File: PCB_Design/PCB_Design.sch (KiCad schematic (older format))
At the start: 10 parts, among them J1 TP4056

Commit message: Hojas en el esquemático
Se añadió como hoja independiente el cargador de la batería al esquemático.
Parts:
- removed BT: Battery_Cell, symbol Device:Battery_Cell
- removed C1, C2: 10u, symbol Device:C
- removed J1: TP4056, SOIC127P600X175-9N, symbol TP4056:TP4056
- removed R_5v: 0.4, symbol Device:R
- removed R_PROG: R, symbol Device:R
- removed R_gLED, R_rLED: 1k, symbol Device:R
- removed gLED, rLED: LED, symbol Device:LED
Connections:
- net labels removed: +5V, GND
- wire segments 25 -> 0
- no-connect marks 2 -> 0

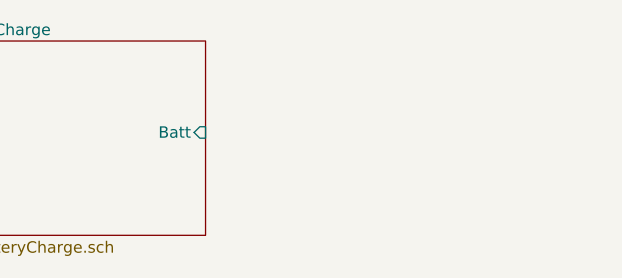
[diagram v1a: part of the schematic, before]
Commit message: Creación de la hoja de regulación de tensión
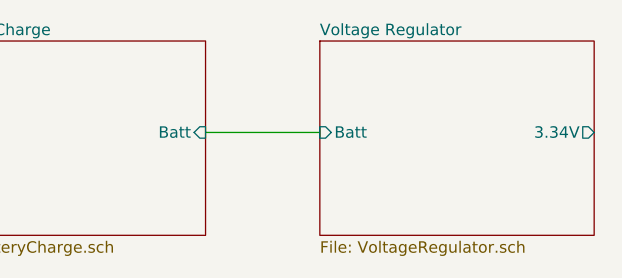
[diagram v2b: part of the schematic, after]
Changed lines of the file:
@@
 $Descr A4 11693 8268
 encoding utf-8
-Sheet 1 2
+Sheet 1 3
 Title ""
 Date ""
@@
 F2 "Batt" I R 3550 2100 50
 $EndSheet
+$Sheet
+S 4050 1700 1200 850
+U 619FB45F
+F0 "Voltage Regulator" 50
+F1 "VoltageRegulator.sch" 50
+F2 "Batt" I L 4050 2100 50
+F3 "3.34V" O R 5250 2100 50
+$EndSheet
+Wire Wire Line
+	3550 2100 4050 2100
 $EndSCHEMATC

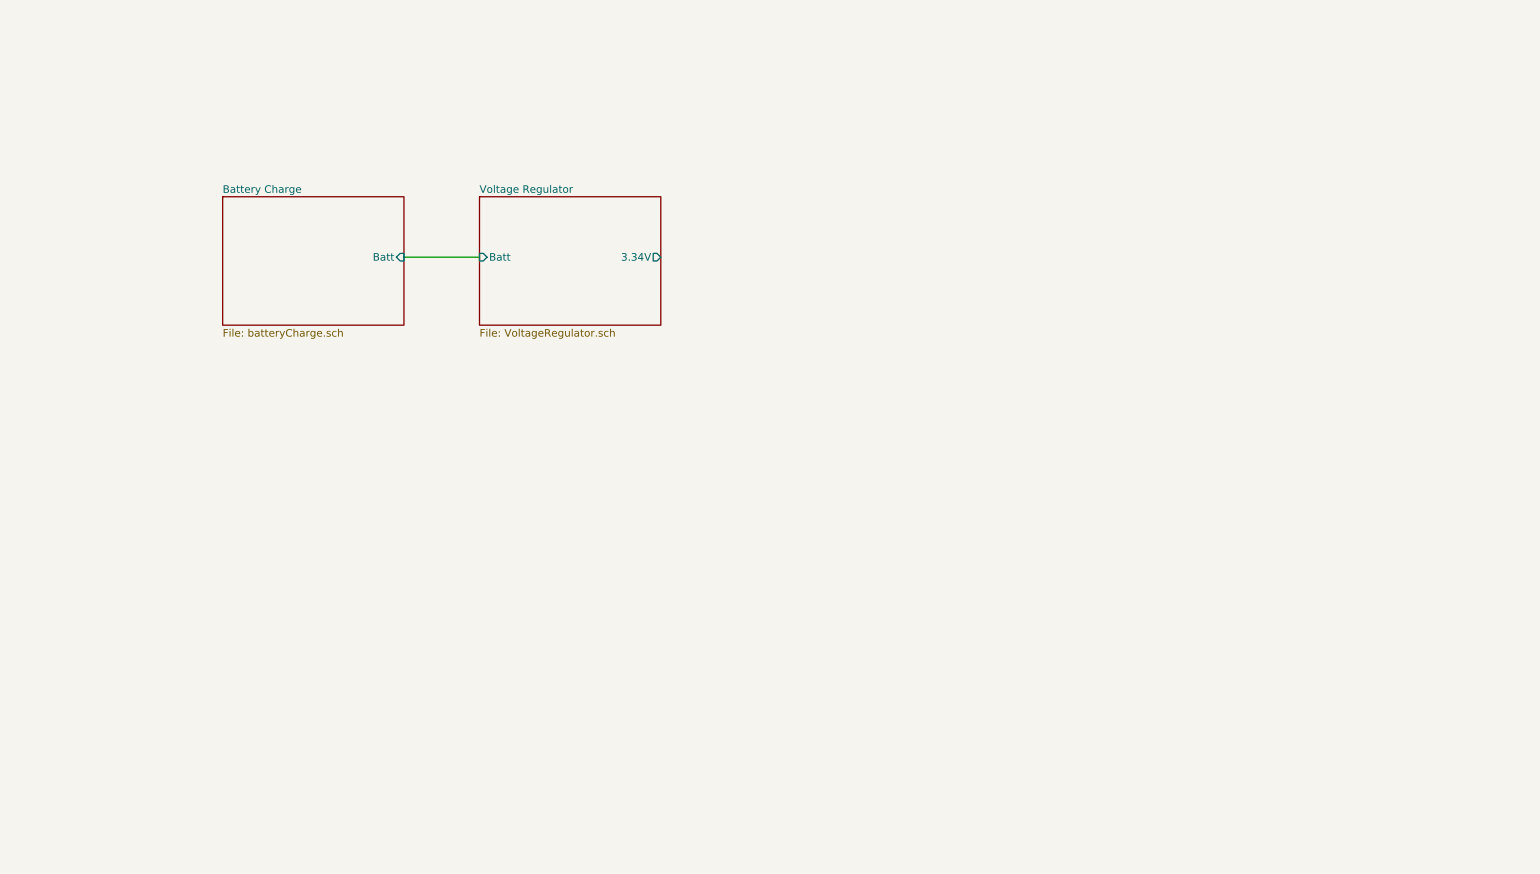
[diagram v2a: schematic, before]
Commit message: Programación por UART-Botones
Se añadieron los botones con el circuito de debouncing, un botón de enable para la esp32 y los pines para la programacion.
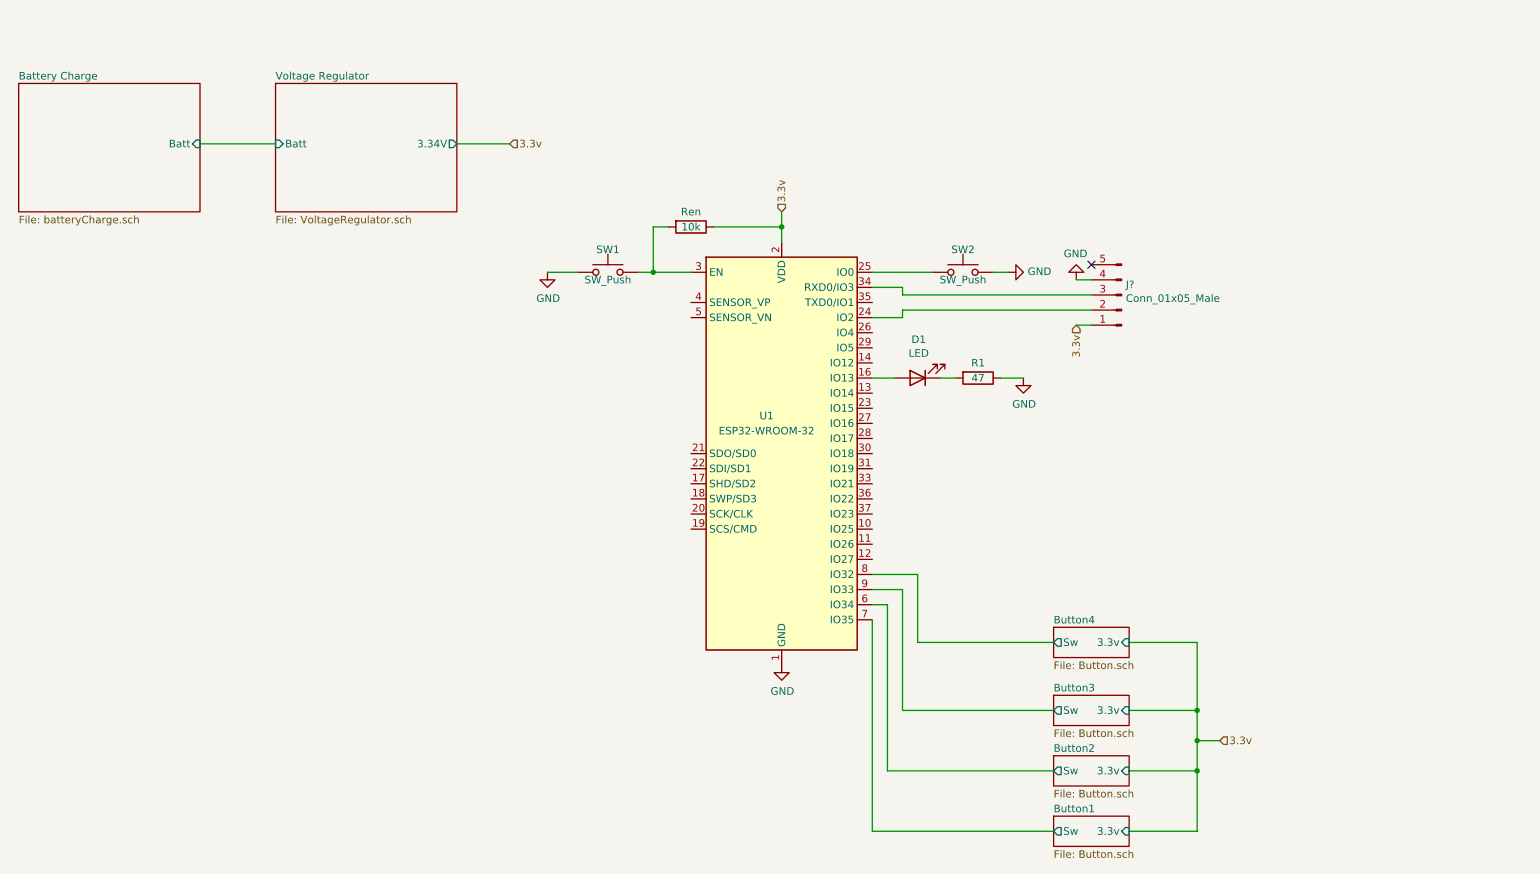
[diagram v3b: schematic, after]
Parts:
- added D1: LED, symbol Device:LED
- added J?: Conn_01x05_Male, symbol Connector:Conn_01x05_Male
- added R1: 47, symbol Device:R
- added Ren: 10k, symbol Device:R
- added SW1, SW2: SW_Push, symbol Switch:SW_Push
- added U1: ESP32-WROOM-32, RF_Module:ESP32-WROOM-32, symbol RF_Module:ESP32-WROOM-32
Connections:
- new net: D1.2 (A), U1.16 (IO13)
- new net: J?.2 (Pin_2), U1.24 (IO2)
- new net: SW2.1, U1.25 (IO0)
- new net: Ren.2, SW1.2, U1.3 (EN)
- new net: J?.3 (Pin_3), U1.34 (RXD0/IO3)
- new net: D1.1 (K), R1.2
- new net 3.3v: J?.1 (Pin_1), Ren.1, U1.2 (VDD)
- new net Button1/Sw: U1.7 (IO35)
- new net Button2 /Sw: U1.6 (IO34)
- new net Button3/Sw: U1.9 (IO33)
- new net Button4/Sw: U1.8 (IO32)
- new net GND: J?.4 (Pin_4), R1.1, SW1.1, SW2.2, U1.1 (GND), U1.15 (GND), U1.38 (GND), U1.39 (GND)
- no-connect marks 0 -> 1

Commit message: Partialy finished schematic
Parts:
- added 4.7k: R_OneWire, symbol Device:R
- added Buzzer: Buzzer, symbol Device:Buzzer
- added Conn_I2C: Conn_01x03_Female, symbol Connector:Conn_01x03_Female
- added Conn_OLED: Conn_01x04_Female, symbol Connector:Conn_01x04_Female
- added D?: LED_RGBC, symbol Device:LED_RGBC
- added LED_Piloto_G: LED, symbol Device:LED
- added NMOS_Buzzer: Q_NMOS_GSD, symbol Device:Q_NMOS_GSD
- added R_Piloto, R_RGB_R: 180, symbol Device:R
- added R_RGB_B, R_RGB_G: 47, symbol Device:R
- added Sens_Temp: DS18B20, Package_TO_SOT_THT:TO-92_Inline, symbol Sensor_Temperature:DS18B20
- gave numbers to parts that had none: 1
- renumbered D1 to LED_Prog_B, R1 to R_Prog_B
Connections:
- net labels added: Batt, One_Wire
- wire segments 43 -> 86
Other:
- moved on the sheet: R_Prog_B

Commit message: huellas agregadas
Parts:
- 4.7k1: renamed from 4.7k; footprint (none) -> Resistor_SMD:R_0805_2012Metric_Pad1.20x1.40mm_HandSolder
- Buzzer1: renamed from Buzzer; footprint (none) -> Buzzer_Beeper:Buzzer_12x9.5RM7.6
- Conn_I2C1: renamed from Conn_I2C; footprint (none) -> Connector_PinSocket_2.54mm:PinSocket_1x03_P2.54mm_Horizontal
- Conn_OLED1: renamed from Conn_OLED; footprint (none) -> Connector_PinSocket_2.54mm:PinSocket_1x04_P2.54mm_Vertical
- Conn_Prog1: renamed from Conn_Prog; footprint (none) -> Connector_PinSocket_2.54mm:PinSocket_1x05_P2.54mm_Horizontal
- D1: renamed from D?; footprint (none) -> LED_THT:LED_D5.0mm-4_RGB_Wide_Pins
- LED_Piloto_G1: renamed from LED_Piloto_G; footprint (none) -> LED_SMD:LED_0805_2012Metric_Pad1.15x1.40mm_HandSolder
- LED_Prog_B1: renamed from LED_Prog_B; footprint (none) -> LED_SMD:LED_0805_2012Metric_Pad1.15x1.40mm_HandSolder
- NMOS_Buzzer1: renamed from NMOS_Buzzer; footprint (none) -> Package_TO_SOT_SMD:SOT-23
- R_Piloto1: renamed from R_Piloto; footprint (none) -> Resistor_SMD:R_0805_2012Metric_Pad1.20x1.40mm_HandSolder
- R_Prog_B1: renamed from R_Prog_B; footprint (none) -> Resistor_SMD:R_0805_2012Metric_Pad1.20x1.40mm_HandSolder
- R_RGB_B1: renamed from R_RGB_B; footprint (none) -> Resistor_SMD:R_0805_2012Metric_Pad1.20x1.40mm_HandSolder
- R_RGB_G1: renamed from R_RGB_G; footprint (none) -> Resistor_SMD:R_0805_2012Metric_Pad1.20x1.40mm_HandSolder
- R_RGB_R1: renamed from R_RGB_R; footprint (none) -> Resistor_SMD:R_0805_2012Metric_Pad1.20x1.40mm_HandSolder
- Ren1: renamed from Ren; footprint (none) -> Resistor_SMD:R_0805_2012Metric_Pad1.20x1.40mm_HandSolder
- SW1, SW2: footprint (none) -> Button_Switch_THT:SW_PUSH_6mm_H5mm
- Sens_Temp1: renamed from Sens_Temp; footprint Package_TO_SOT_THT:TO-92_Inline -> Connector_JST:JST_XH_B3B-XH-A_1x03_P2.50mm_Vertical; symbol Sensor_Temperature:DS18B20 -> PCB_Design-rescue:DS18B20-Sensor_Temperature
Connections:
- net labels removed: One_Wire
- wire segments 86 -> 93
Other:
- moved on the sheet: 4.7k1, Buzzer1, Conn_I2C1, Conn_OLED1, Conn_Prog1, D1, LED_Piloto_G1, LED_Prog_B1, NMOS_Buzzer1, R_Piloto1, R_Prog_B1, R_RGB_B1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

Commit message: huellas editadas
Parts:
- removed Conn_Prog1: Conn_01x05_Male, Connector_PinSocket_2.54mm:PinSocket_1x05_P2.54mm_Horizontal, symbol Connector:Conn_01x05_Male
- added Conn_prog1: Conn_01x05_Female, Connector_PinSocket_2.54mm:PinSocket_1x05_P2.54mm_Horizontal, symbol Connector:Conn_01x05_Female
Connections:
- net 3.3v: now also Conn_prog1.1 (Pin_1)
- net GND: now also Conn_prog1.4 (Pin_4)
- net at U1.34 (RXD0/IO3): now also Conn_prog1.2 (Pin_2)
- net at U1.35 (TXD0/IO1): now also Conn_prog1.3 (Pin_3)
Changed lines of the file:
@@
 Text HLabel 4580 1450 1    50   Input ~ 0
 3.3v
-$Comp
-L Connector:Conn_01x05_Male Conn_Prog1
-U 1 1 61AAC0B7
-P 4845 1905
-F 0 "Conn_Prog1" H 4817 1837 50  0000 R CNN
-F 1 "Conn_01x05_Male" H 4817 1928 50  0000 R CNN
-F 2 "Connector_PinSocket_2.54mm:PinSocket_1x05_P2.54mm_Horizontal" H 4845 1905 50  0001 C CNN
-F 3 "~" H 4845 1905 50  0001 C CNN
-	1    4845 1905
-	-1   0    0    -1
-$EndComp
 Wire Wire Line
 	1745 1705 1995 1705
@@
 Wire Wire Line
 	7480 1440 7200 1440
+$Comp
+L Connector:Conn_01x05_Female Conn_prog1
+U 1 1 61AC4E61
+P 4845 1905
+F 0 "Conn_prog1" H 4873 1931 50  0000 L CNN
+F 1 "Conn_01x05_Female" H 4873 1840 50  0000 L CNN
+F 2 "Connector_PinSocket_2.54mm:PinSocket_1x05_P2.54mm_Horizontal" H 4845 1905 50  0001 C CNN
+F 3 "~" H 4845 1905 50  0001 C CNN
+	1    4845 1905
+	1    0    0    -1
+$EndComp
 $EndSCHEMATC

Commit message: Falta tetris
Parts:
- U1: symbol RF_Module:ESP32-WROOM-32 -> PCB_Design-rescue:ESP32-WROOM-32-RF_Module
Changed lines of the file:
@@
 $EndSheet
 $Comp
-L RF_Module:ESP32-WROOM-32 U1
+L PCB_Design-rescue:ESP32-WROOM-32-RF_Module U1
 U 1 1 61A64564
 P 2595 2905

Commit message: Nuevas huellas y un poco más de orden
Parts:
- SW1, SW2: footprint Button_Switch_THT:SW_PUSH_6mm_H5mm -> Button_Switch_SMD:SW_SPST_B3U-1000P
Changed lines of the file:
@@
 F 0 "SW1" H 1445 1855 50  0000 C CNN
 F 1 "SW_Push" H 1445 1655 50  0000 C CNN
-F 2 "Button_Switch_THT:SW_PUSH_6mm_H5mm" H 1445 1905 50  0001 C CNN
+F 2 "Button_Switch_SMD:SW_SPST_B3U-1000P" H 1445 1905 50  0001 C CNN
 F 3 "~" H 1445 1905 50  0001 C CNN
 	1    1445 1705
@@
 F 0 "SW2" H 3795 1855 50  0000 C CNN
 F 1 "SW_Push" H 3795 1655 50  0000 C CNN
-F 2 "Button_Switch_THT:SW_PUSH_6mm_H5mm" H 3795 1905 50  0001 C CNN
+F 2 "Button_Switch_SMD:SW_SPST_B3U-1000P" H 3795 1905 50  0001 C CNN
 F 3 "~" H 3795 1905 50  0001 C CNN
 	1    3795 1705
